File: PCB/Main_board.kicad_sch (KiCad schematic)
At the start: 212 parts, among them J1 USB_C_Receptacle_USB2.0_14P, J2 Conn_02x03_Odd_Even, Q1 Q_PMOS_GSD, Q2 Q_PMOS_GSD, Q3 Q_PMOS_GSD, SW1 SW_Push, SW10 SW_Push, SW11 SW_Push, SW12 SW_Push, SW13 SW_Push, SW14 SW_Push, SW15 SW_Push, SW16 SW_Push, SW17 SW_Push, SW18 SW_Push, SW19 SW_Push, SW2 SW_Push, SW20 SW_Push, SW21 SW_Push, SW22 SW_Push, SW23 SW_Push, SW24 SW_Push, SW25 SW_Push, SW26 SW_Push, SW27 SW_Push, SW28 SW_Push, SW29 SW_Push, SW3 SW_Push, SW30 SW_Push, SW31 SW_Push, SW32 SW_Push, SW33 SW_Push, SW34 SW_Push, SW35 SW_Push, SW36 SW_Push, SW37 SW_Push, SW38 SW_Push, SW39 SW_Push, SW4 SW_Push, SW40 SW_Push, SW41 SW_Push, SW42 SW_Push, SW43 SW_Push, SW44 SW_Push, SW45 SW_Push, SW46 SW_Push, SW47 SW_Push, SW48 SW_Push, SW49 SW_Push, SW5 SW_Push, SW50 SW_Push, SW51 SW_Push, SW52 SW_Push, SW53 SW_Push, SW54 SW_Push, SW55 SW_Push, SW56 SW_Push, SW57 SW_Push, SW58 SW_Push, SW59 SW_Push, SW6 SW_Push, SW60 SW_Push, SW61 SW_Push, SW62 SW_Push, SW63 SW_Push, SW64 SW_Push, SW65 SW_Push, SW66 SW_Push, SW67 SW_Push, SW68 SW_Push, SW69 SW_Push, SW7 SW_Push, SW70 SW_Push, SW71 SW_Push, SW72 SW_Push, SW73 SW_Push, SW74 SW_Push, SW75 SW_Push, SW76 SW_Push, SW77 SW_Push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

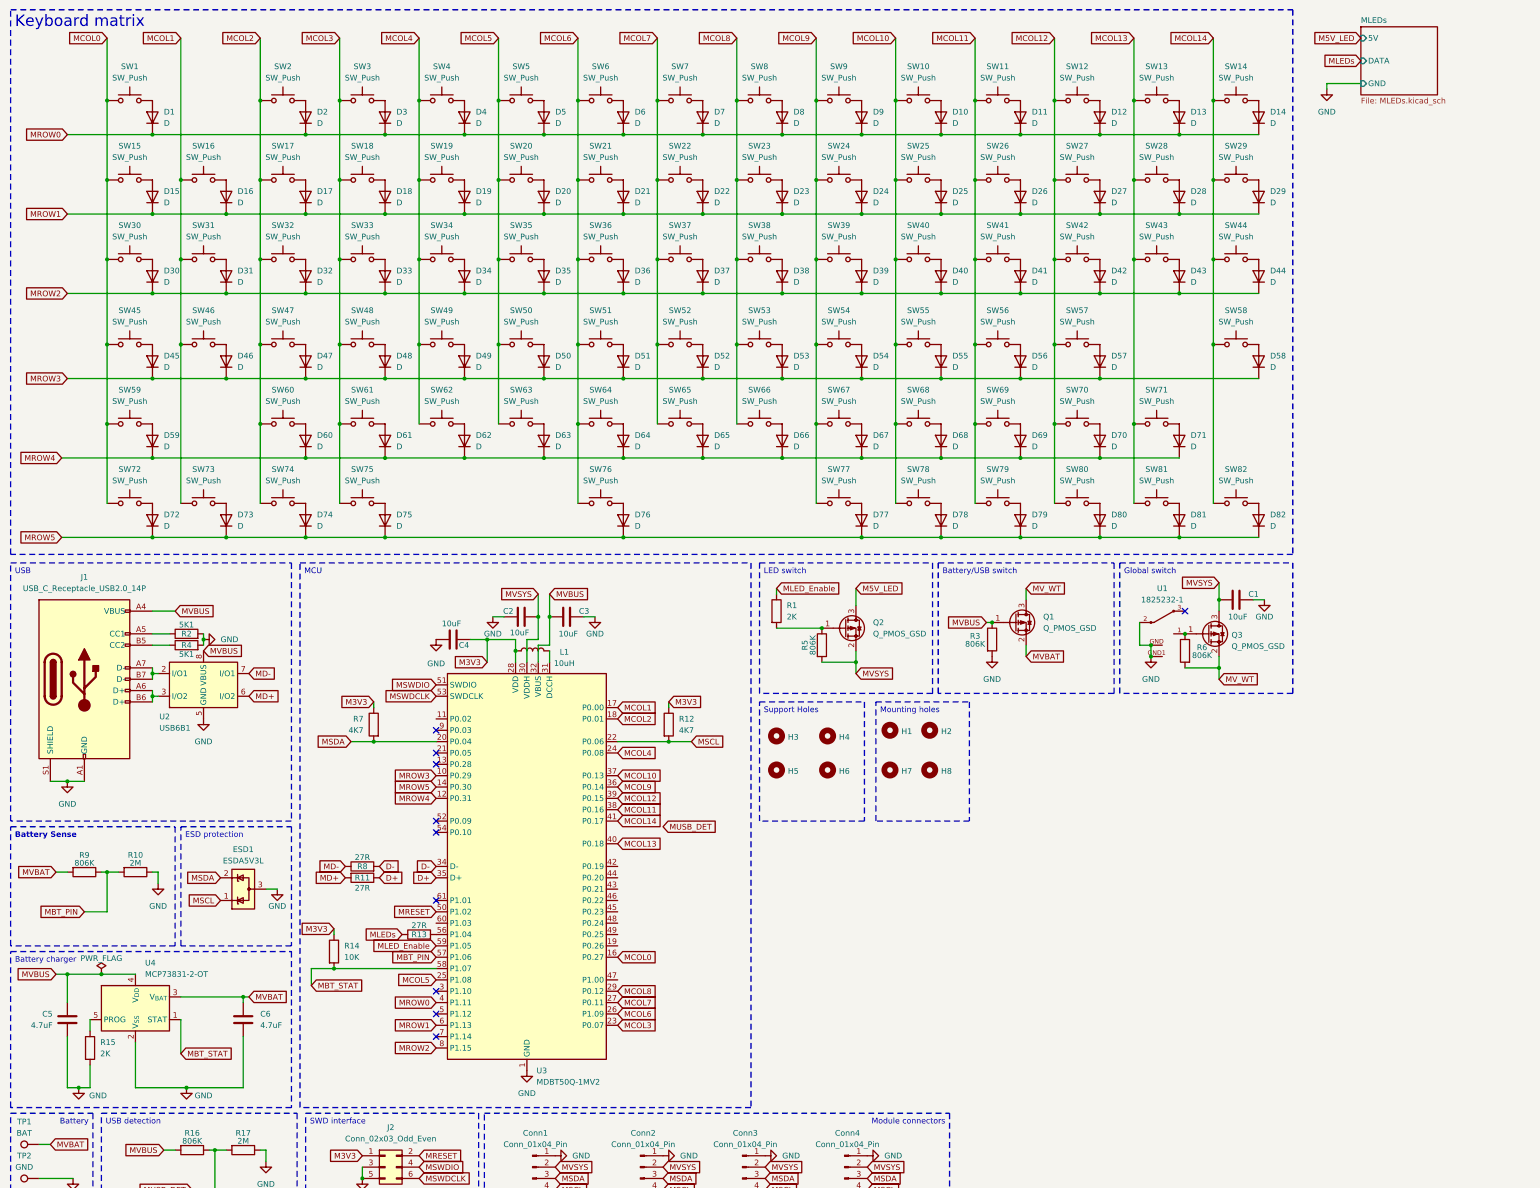
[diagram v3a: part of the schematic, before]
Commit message: Update: schematic and PCB
Replaced the MT3608 module with a custom circuit for it.
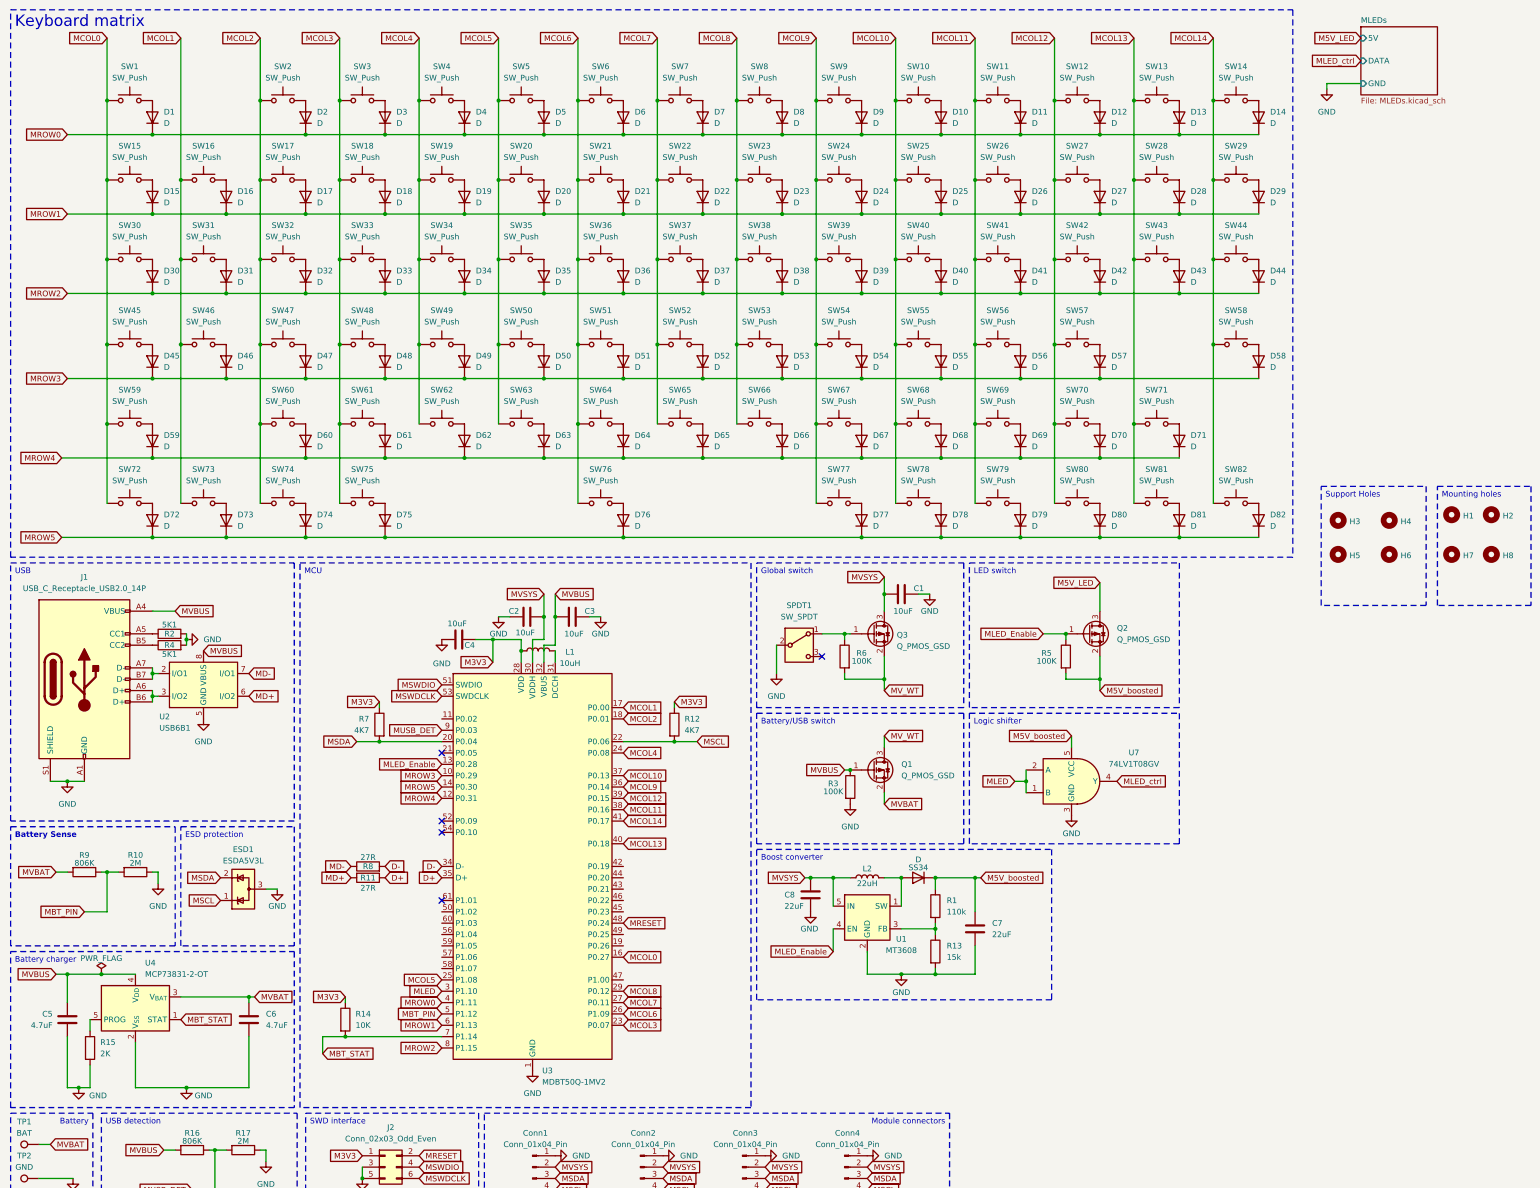
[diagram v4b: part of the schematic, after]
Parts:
- removed U1: 1825232-1, Footprints:1825232-1, symbol 1825232-1:1825232-1
- added C7, C8: 22uF, Capacitor_SMD:C_1206_3216Metric, symbol Device:C
- added L2: 22uH, Footprints:IND-SMD_L7.1-W6.6, symbol Device:L
- added SPDT1: SW_SPDT, Footprints:1825232-1, symbol Switch:SW_SPDT
- added SS34: D, Footprints:SS34, symbol Device:D
- added U1: MT3608, Package_TO_SOT_SMD:SOT-23-6, symbol Regulator_Switching:MT3608
- added U7: 74LV1T08GV, Package_TO_SOT_SMD:SC-74A-5_1.55x2.9mm_P0.95mm, symbol 74xx:74LV1T08GV
- R1: value 2K -> 110k; LCSC Part # C17604 -> (none); Link https://jlcpcb.com/partdetail/C17604 -> (none); Unit Price ($) 0.01 -> (none)
- R13: value 27R -> 15k; LCSC Part # C17594 -> (none); Link https://jlcpcb.com/partdetail/C17594 -> (none); Unit Price ($) 0.01 -> (none)
- R3, R5, R6: value 806K -> 100K
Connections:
- net GND: now also R13.2, C7.2, C8.2, SPDT1.2 (B), U1.2 (GND), U7.3 (GND)
- net MBT_PIN: now also U3.5 (P1.12); no longer U3.57 (P1.06)
- net MBT_STAT: now also U3.7 (P1.14); no longer U3.58 (P1.07)
- net MLED_Enable: now also Q2.1 (G), R5.1, U3.13 (P0.28), U1.4 (EN); no longer R1.1, U3.59 (P1.05)
- net MRESET: now also U3.48 (P0.24); no longer U3.50 (P1.02)
- net MUSB_DET: now also U3.9 (P0.03)
- net MVSYS: now also C8.1, L2.1, U1.5 (IN); no longer Q2.2 (S), R5.2
- net at U3.56 (P1.04): no longer R13.2
- net at Q3.1 (G), R6.1: now also SPDT1.1 (A)
- net MLED: now reaches U3.3 (P1.10)
- net MLED: now also U7.1 (B), U7.2 (A)
- net MLEDs: no longer names the net of R13.1
- net MLEDs: now also R1.2, U1.3 (FB)
- new net: L2.2, SS34.2 (A), U1.1 (SW)
- new net M5V_boosted: C7.1, Q2.2 (S), R1.1, R5.2, SS34.1 (K), U7.5 (VCC)
- new net MLED_ctrl: U7.4 (Y)
- no-connect marks 10 -> 5
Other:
- moved on the sheet: C1, C2, C3, C4, C6, H1, H2, H3, H4, H5, H6, H7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

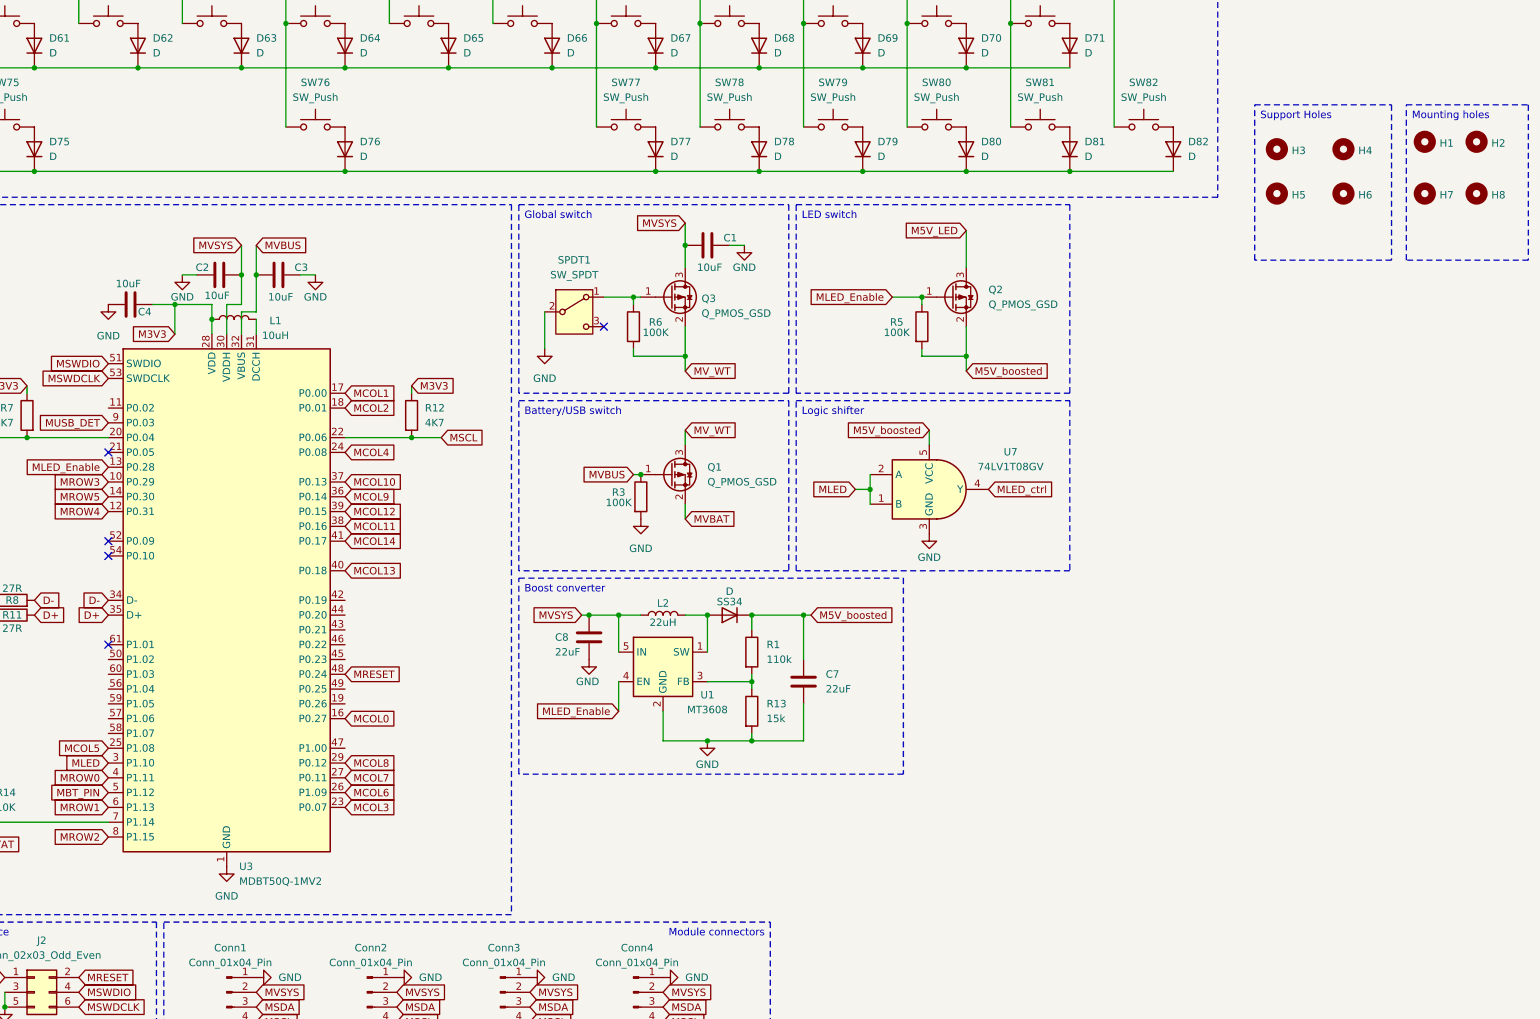
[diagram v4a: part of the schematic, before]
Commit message: Update: change footprint to V1V2, update 3D models, Add rotary encoder and 128x32 OLED, Remove second 128x64 OLED
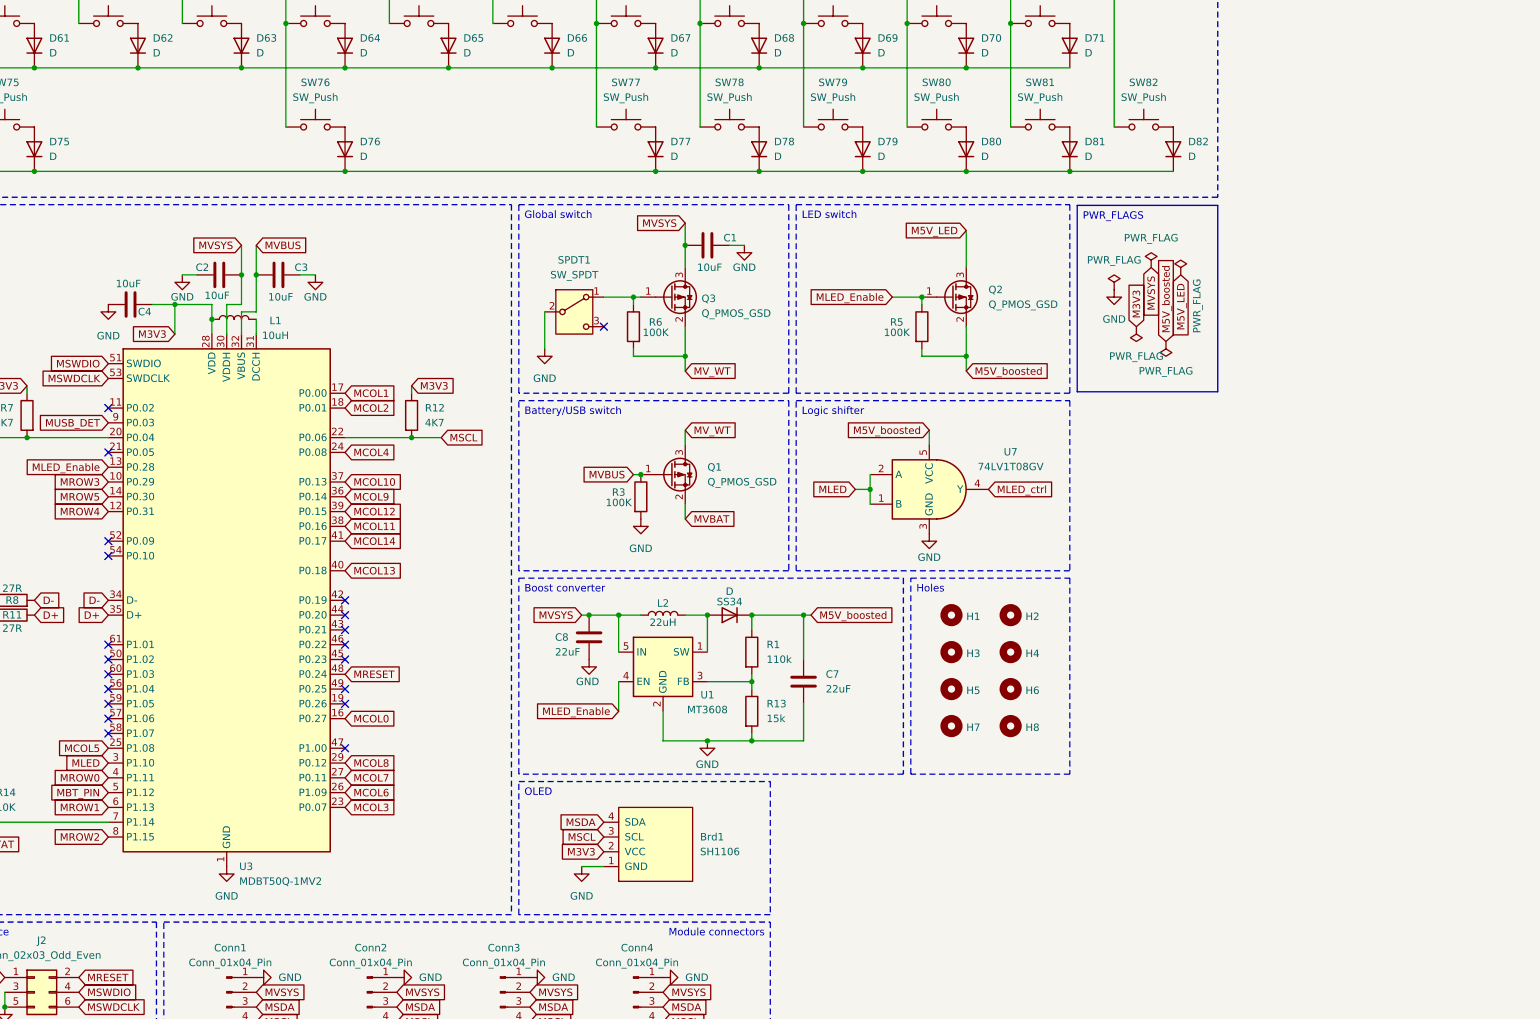
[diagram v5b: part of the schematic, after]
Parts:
- added Brd1: SH1106, Footprints:OLED-TH_L38.0-W12.0_HS91L02W2C01, symbol SSD1306-128x64_OLED:SSD1306
- SW1, SW10, SW11, SW12, SW13, SW14, SW15, SW16, SW17, SW18, SW19, SW2, SW20, SW21, SW22, SW23, SW24, SW25, SW26, SW27, SW29, SW3, SW31, SW32, SW33, SW34, SW35, SW36, SW37, SW38, SW39, SW4, SW40, SW41, SW42, SW44, SW46, SW47, SW48, SW49, SW5, SW50, SW51, SW52, SW53, SW54, SW55, SW56, SW58, SW6, SW60, SW61, SW62, SW63, SW64, SW65, SW66, SW67, SW68, SW69, SW7, SW71, SW72, SW73, SW74, SW75, SW77, SW78, SW79, SW8, SW80, SW81, SW82, SW9: footprint Footprints:Kailh_choc_HS_V2_1u -> Footprints:Kailh_choc_HS_V1V2_1u
- SW28: footprint Footprints:Kailh_choc_HS_V2_2u -> Footprints:Kailh_choc_HS_V1V2_2u
- SW30, SW43: footprint Footprints:Kailh_choc_HS_V2_1.5u -> Footprints:Kailh_choc_HS_V1V2_1.5u
- SW45, SW70: footprint Footprints:Kailh_choc_HS_V2_1.75u -> Footprints:Kailh_choc_HS_V1V2_1.75u
- SW57, SW59: footprint Footprints:Kailh_choc_HS_V2_2.25u -> Footprints:Kailh_choc_HS_V1V2_2.25u
- SW76: footprint Footprints:Kailh_choc_HS_V2_6u -> Footprints:Kailh_choc_HS_V1V2_6u
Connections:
- net GND: now also Brd1.1 (GND)
- net M3V3: now also Brd1.2 (VCC)
- net MSCL: now also Brd1.3 (SCL)
- net MSDA: now also Brd1.4 (SDA)
- no-connect marks 5 -> 20
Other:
- moved on the sheet: H1, H2, H3, H4, H5, H6, H7, H8

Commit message: Update: Changed keyswitch footprints to HS MX switches
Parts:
- Conn1, Conn3: footprint Connector_PinHeader_2.54mm:PinHeader_1x04_P2.54mm_Vertical -> Footprints:Pogopin_Conn_1x4_Female
- Conn2, Conn4: footprint Connector_PinHeader_2.54mm:PinHeader_1x04_P2.54mm_Vertical -> Footprints:Pogopin_Conn_1x4_Male
- SW1, SW10, SW11, SW12, SW13, SW14, SW15, SW16, SW17, SW18, SW19, SW2, SW20, SW21, SW22, SW23, SW24, SW25, SW26, SW27, SW29, SW3, SW31, SW32, SW33, SW34, SW35, SW36, SW37, SW38, SW39, SW4, SW40, SW41, SW42, SW44, SW46, SW47, SW48, SW49, SW5, SW50, SW51, SW52, SW53, SW54, SW55, SW56, SW58, SW6, SW60, SW61, SW62, SW63, SW64, SW65, SW66, SW67, SW68, SW69, SW7, SW71, SW72, SW73, SW74, SW75, SW77, SW78, SW79, SW8, SW80, SW81, SW82, SW9: footprint Footprints:Kailh_choc_HS_V1V2_1u -> Footprints:MX_HS_1u
- SW28: footprint Footprints:Kailh_choc_HS_V1V2_2u -> Footprints:MX_HS_2u
- SW30, SW43: footprint Footprints:Kailh_choc_HS_V1V2_1.5u -> Footprints:MX_HS_1.5u
- SW45, SW70: footprint Footprints:Kailh_choc_HS_V1V2_1.75u -> Footprints:MX_HS_1.75u
- SW57, SW59: footprint Footprints:Kailh_choc_HS_V1V2_2.25u -> Footprints:MX_HS_2.25u
- SW76: footprint Footprints:Kailh_choc_HS_V1V2_6u -> Footprints:MX_HS_6u

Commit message: Init: Keyboard Case
Development only
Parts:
- H1, H2, H3, H4, H5, H6, H7, H8: footprint MountingHole:MountingHole_2.2mm_M2 -> MountingHole:MountingHole_3.2mm_M3
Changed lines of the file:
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@@
 			)
 		)
-		(property "Footprint" "MountingHole:MountingHole_2.2mm_M2"
+		(property "Footprint" "MountingHole:MountingHole_3.2mm_M3"
 			(at 266.7 228.6 0)
 			(effects
@@
 			)
 		)
-		(property "Footprint" "MountingHole:MountingHole_2.2mm_M2"
+		(property "Footprint" "MountingHole:MountingHole_3.2mm_M3"
 			(at 256.54 222.25 0)
 			(effects
@@
 			)
 		)
-		(property "Footprint" "MountingHole:MountingHole_2.2mm_M2"
+		(property "Footprint" "MountingHole:MountingHole_3.2mm_M3"
 			(at 266.7 209.55 0)
 			(effects
@@
 			)
 		)
-		(property "Footprint" "MountingHole:MountingHole_2.2mm_M2"
+		(property "Footprint" "MountingHole:MountingHole_3.2mm_M3"
 			(at 256.54 209.55 0)
 			(effects
@@
 			)
 		)
-		(property "Footprint" "MountingHole:MountingHole_2.2mm_M2"
+		(property "Footprint" "MountingHole:MountingHole_3.2mm_M3"
 			(at 256.54 228.6 0)
 			(effects
@@
 			)
 		)
-		(property "Footprint" "MountingHole:MountingHole_2.2mm_M2"
+		(property "Footprint" "MountingHole:MountingHole_3.2mm_M3"
 			(at 266.7 215.9 0)
 			(effects
@@
 			)
 		)
-		(property "Footprint" "MountingHole:MountingHole_2.2mm_M2"
+		(property "Footprint" "MountingHole:MountingHole_3.2mm_M3"
 			(at 266.7 222.25 0)
 			(effects
@@
 			)
 		)
-		(property "Footprint" "MountingHole:MountingHole_2.2mm_M2"
+		(property "Footprint" "MountingHole:MountingHole_3.2mm_M3"
 			(at 256.54 215.9 0)
 			(effects

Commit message: Update README.md
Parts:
- Conn1, Conn2, Conn3, Conn4: Name (none) -> Connectors
- L1: Name (none) -> Inductors
- Q1, Q2, Q3: Name (none) -> P_Mosfets
- SPDT1: Name (none) -> Slide Switch
- SS34: Name (none) -> Diode
- U1: Name (none) -> MT3608
- U7: Name (none) -> 74LV1T08GV
